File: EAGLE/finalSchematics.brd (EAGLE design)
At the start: 100 x 80 mm, 12 parts, among them IC1 STM32F103RBT, P1 DM3CS-SF, Q1 8MHz 131-220

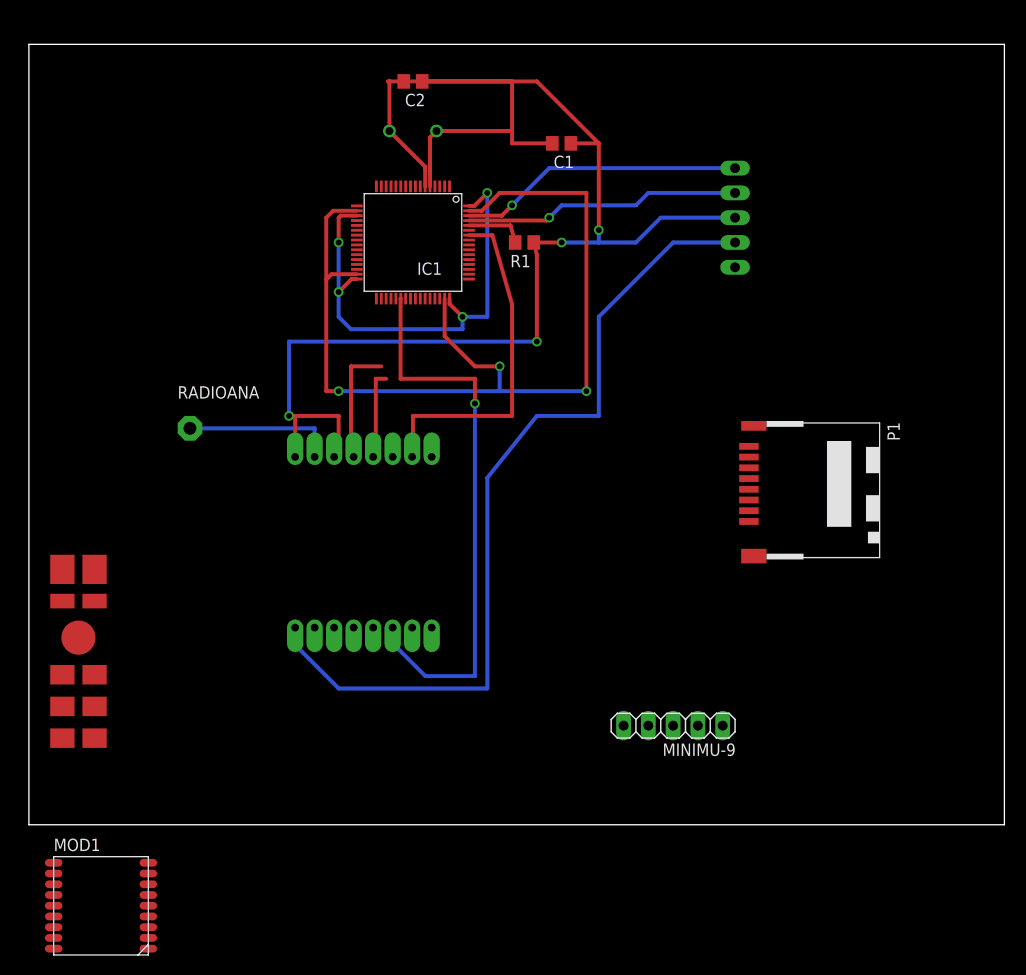
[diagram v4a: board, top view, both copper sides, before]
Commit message: Finish modules
All modules except SD card imported in the schematic. Board still to-do
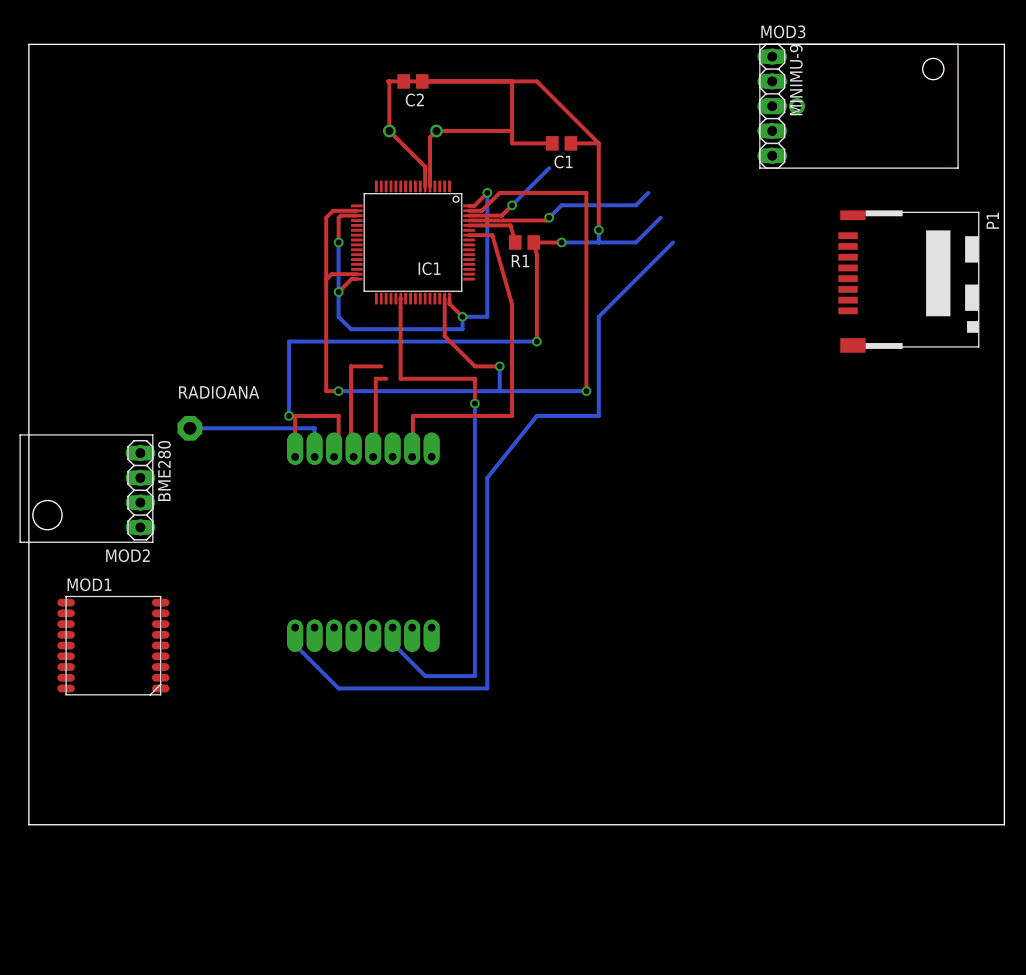
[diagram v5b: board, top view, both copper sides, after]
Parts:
- removed GPSANA: ANT-NSG4712-6, roundsolutions:ANT-NSG4712-6
- added MOD2: (no value), BME280:BME280
- added MOD3: IMU04A, IMU:IMU04A
- BME280: device pinhead:1X05/90 -> pinhead:1X04
- MOD1: value (none) -> GPS
- moved BME280 70.5 mm to (11.4, 34.3), flipped to the top, turned to 270 degrees
- moved MINIMU-9 64.3 mm to (76.2, 73.7), turned to 270 degrees
- moved MOD1 26.7 mm to (3.81, 14.0)
- moved P1 23.9 mm to (90.2, 55.9)
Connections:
- new net RX: MOD1.RXD1
- new net TX: MOD1.TXD1
- net +3V3: now also BME280.1; no longer BME280.2
- net GND: now also BME280.2; no longer BME280.3
- net SCL: now also BME280.3; no longer BME280.4
- net SDA: now also BME280.4; no longer BME280.5
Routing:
- net SDA: track 29.3 -> 10.2 mm
- net SCL: track 77.6 -> 68.7 mm
- net GND: track 113.2 -> 105.6 mm
- net +3V3: track 87.2 -> 80.8 mm
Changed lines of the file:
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@@
 <?xml version="1.0" encoding="utf-8"?>
 <!DOCTYPE eagle SYSTEM "eagle.dtd">
-<eagle version="8.0.1">
+<eagle version="8.0.0">
 <drawing>
 <settings>
@@
 <element name="R1" library="rcl" package="R0805" value="10k 901-655" x="50.8" y="59.69" rot="R180"/>
 <element name="U$1" library="RFM69mod" package="20X16BOARD" value="RFM69" x="34.29" y="29.21" rot="MR90"/>
-<element name="BME280" library="pinhead" package="1X05/90" value="" x="76.2" y="62.23" rot="MR90"/>
-<element name="GPSANA" library="roundsolutions" package="ANT-NSG4712-6" value="ANT-NSG4712-6" x="5.08" y="17.78"/>
-<element name="MINIMU-9" library="pinhead" package="1X05" value="" x="66.04" y="10.16" rot="R180"/>
-<element name="P1" library="DM3CS-SF" package="HRS_DM3CS-SF" value="DM3CS-SF" x="80.01" y="34.29" rot="R270">
-<attribute name="PRICE" value="1.04 USD" x="80.01" y="34.29" size="1.778" layer="27" rot="R270" display="off"/>
-<attribute name="DESCRIPTION" value="Conn Micro SD Card HDR 8 POS 1.1mm Solder RA SMD Embossed T/R 0.5A" x="80.01" y="34.29" size="1.778" layer="27" rot="R270" display="off"/>
-<attribute name="MP" value="DM3CS-SF" x="80.01" y="34.29" size="1.778" layer="27" rot="R270" display="off"/>
-<attribute name="AVAILABILITY" value="Good" x="80.01" y="34.29" size="1.778" layer="27" rot="R270" display="off"/>
-<attribute name="PACKAGE" value="None" x="80.01" y="34.29" size="1.778" layer="27" rot="R270" display="off"/>
-<attribute name="MF" value="Hirose" x="80.01" y="34.29" size="1.778" layer="27" rot="R270" display="off"/>
+<element name="MINIMU-9" library="pinhead" package="1X05" value="" x="76.2" y="73.66" rot="R270"/>
+<element name="P1" library="DM3CS-SF" package="HRS_DM3CS-SF" value="DM3CS-SF" x="90.17" y="55.88" rot="R270">
+<attribute name="PRICE" value="1.04 USD" x="90.17" y="55.88" size="1.778" layer="27" rot="R270" display="off"/>
+<attribute name="DESCRIPTION" value="Conn Micro SD Card HDR 8 POS 1.1mm Solder RA SMD Embossed T/R 0.5A" x="90.17" y="55.88" size="1.778" layer="27" rot="R270" display="off"/>
+<attribute name="MP" value="DM3CS-SF" x="90.17" y="55.88" size="1.778" layer="27" rot="R270" display="off"/>
+<attribute name="AVAILABILITY" value="Good" x="90.17" y="55.88" size="1.778" layer="27" rot="R270" display="off"/>
+<attribute name="PACKAGE" value="None" x="90.17" y="55.88" size="1.778" layer="27" rot="R270" display="off"/>
+<attribute name="MF" value="Hirose" x="90.17" y="55.88" size="1.778" layer="27" rot="R270" display="off"/>
 </element>
-<element name="MOD1" library="components" package="L70B-GPS" value="" x="2.54" y="-12.7"/>
+<element name="MOD1" library="components" package="L70B-GPS" value="GPS" x="3.81" y="13.97"/>
+<element name="MOD2" library="BME280" package="BME280" value="" x="12.7" y="39.37" rot="R180"/>
+<element name="BME280" library="pinhead" package="1X04" value="" x="11.43" y="34.29" rot="R270"/>
+<element name="MOD3" library="IMU" package="IMU04A" value="IMU04A" x="76.2" y="73.66"/>
 </elements>
 <signals>
@@
 <wire x1="26.67" y1="49.53" x2="26.67" y2="41.91" width="0.4064" layer="16"/>
 <via x="26.67" y="41.91" extent="1-16" drill="0.6"/>
-<contactref element="BME280" pad="3"/>
 <via x="52.07" y="49.53" extent="1-16" drill="0.6" shape="square"/>
 <wire x1="52.07" y1="58.42" x2="51.75" y2="59.69" width="0.4064" layer="1"/>
@@
 <wire x1="58.42" y1="59.69" x2="62.23" y2="59.69" width="0.4064" layer="16"/>
 <wire x1="62.23" y1="59.69" x2="64.77" y2="62.23" width="0.4064" layer="16"/>
-<wire x1="64.77" y1="62.23" x2="72.39" y2="62.23" width="0.4064" layer="16"/>
 <wire x1="58.42" y1="59.69" x2="58.42" y2="60.96" width="0.4064" layer="16"/>
 <via x="58.42" y="60.96" extent="1-16" drill="0.6" shape="square"/>
@@
 <contactref element="MINIMU-9" pad="3"/>
 <contactref element="P1" pad="6"/>
+<contactref element="BME280" pad="2"/>
+<contactref element="MOD1" pad="GND2"/>
 <contactref element="MOD1" pad="GND1"/>
-<contactref element="MOD1" pad="GND2"/>
 <contactref element="MOD1" pad="GND3"/>
-<wire x1="52.07" y1="49.53" x2="73.81" y2="36.59" width="0" layer="19" extent="1-1"/>
-<wire x1="66.04" y1="10.16" x2="73.81" y2="36.59" width="0" layer="19" extent="1-1"/>
-<wire x1="2.54" y1="-3.9" x2="27.29" y2="37.71" width="0" layer="19" extent="1-1"/>
-<wire x1="2.54" y1="-6.1" x2="2.54" y2="-3.9" width="0" layer="19" extent="1-1"/>
-<wire x1="12.24" y1="-12.7" x2="2.54" y2="-6.1" width="0" layer="19" extent="1-1"/>
+<wire x1="52.07" y1="49.53" x2="83.97" y2="58.18" width="0" layer="19" extent="1-1"/>
+<wire x1="76.2" y1="73.66" x2="83.97" y2="58.18" width="0" layer="19" extent="1-1"/>
+<wire x1="3.81" y1="22.77" x2="27.29" y2="37.71" width="0" layer="19" extent="1-1"/>
+<wire x1="3.81" y1="20.57" x2="3.81" y2="22.77" width="0" layer="19" extent="1-1"/>
+<wire x1="13.51" y1="13.97" x2="3.81" y2="20.57" width="0" layer="19" extent="1-1"/>
+<wire x1="11.43" y1="35.56" x2="13.51" y2="13.97" width="0" layer="19" extent="1-1"/>
 </signal>
 <signal name="NC">
@@
 <signal name="+3V3">
 <contactref element="U$1" pad="3.3V"/>
-<contactref element="BME280" pad="2"/>
-<wire x1="72.39" y1="59.69" x2="66.04" y2="59.69" width="0.4064" layer="16"/>
 <wire x1="66.04" y1="59.69" x2="58.42" y2="52.07" width="0.4064" layer="16"/>
 <wire x1="58.42" y1="52.07" x2="58.42" y2="41.91" width="0.4064" layer="16"/>
@@
 <contactref element="P1" pad="4"/>
 <contactref element="MINIMU-9" pad="5"/>
-<wire x1="60.96" y1="10.16" x2="73.81" y2="34.39" width="0" layer="19" extent="1-1"/>
-<wire x1="33.02" y1="13.97" x2="60.96" y2="10.16" width="0" layer="19" extent="16-16"/>
+<contactref element="BME280" pad="1"/>
+<wire x1="58.42" y1="41.91" x2="83.97" y2="55.98" width="0" layer="19" extent="1-16"/>
+<wire x1="76.2" y1="68.58" x2="46.99" y2="13.97" width="0" layer="19" extent="16-16"/>
+<wire x1="11.43" y1="38.1" x2="31.75" y2="13.97" width="0" layer="19" extent="16-16"/>
 </signal>
 <signal name="SCL">
@@
 <contactref element="MINIMU-9" pad="1"/>
 <contactref element="IC1" pad="61"/>
-<contactref element="BME280" pad="4"/>
 <wire x1="45.12" y1="61.94" x2="53.05" y2="61.94" width="0.4064" layer="1"/>
 <wire x1="53.05" y1="61.94" x2="53.34" y2="62.23" width="0.4064" layer="1"/>
@@
 <wire x1="54.61" y1="63.5" x2="62.23" y2="63.5" width="0.4064" layer="16"/>
 <wire x1="62.23" y1="63.5" x2="63.5" y2="64.77" width="0.4064" layer="16"/>
-<wire x1="63.5" y1="64.77" x2="72.39" y2="64.77" width="0.4064" layer="16"/>
+<contactref element="BME280" pad="3"/>
 <wire x1="45.12" y1="63.44" x2="45.12" y2="61.94" width="0" layer="19" extent="1-1"/>
-<wire x1="71.12" y1="10.16" x2="33.02" y2="50.8" width="0" layer="19" extent="16-16"/>
+<wire x1="76.2" y1="78.74" x2="46.99" y2="52.07" width="0" layer="19" extent="16-16"/>
+<wire x1="11.43" y1="33.02" x2="76.2" y2="78.74" width="0" layer="19" extent="1-1"/>
 </signal>
 <signal name="SDA">
 <contactref element="MINIMU-9" pad="2"/>
 <contactref element="IC1" pad="62"/>
-<contactref element="BME280" pad="5"/>
 <wire x1="45.12" y1="62.44" x2="48.47" y2="62.44" width="0.4064" layer="1"/>
 <wire x1="48.47" y1="62.44" x2="49.53" y2="63.5" width="0.4064" layer="1"/>
 <via x="49.53" y="63.5" extent="1-16" drill="0.6" shape="square"/>
 <wire x1="49.53" y1="63.5" x2="53.34" y2="67.31" width="0.4064" layer="16"/>
-<wire x1="53.34" y1="67.31" x2="72.39" y2="67.31" width="0.4064" layer="16"/>
-<wire x1="68.58" y1="10.16" x2="45.12" y2="62.44" width="0" layer="19" extent="1-1"/>
+<contactref element="BME280" pad="4"/>
+<wire x1="76.2" y1="76.2" x2="48.47" y2="62.44" width="0" layer="19" extent="1-1"/>
+<wire x1="11.43" y1="30.48" x2="76.2" y2="76.2" width="0" layer="19" extent="1-1"/>
 </signal>
 <signal name="MOSI">
 <contactref element="P1" pad="3"/>
 <contactref element="IC1" pad="36"/>
-<wire x1="73.81" y1="33.29" x2="37.12" y2="53.94" width="0" layer="19" extent="1-1"/>
+<wire x1="83.97" y1="54.88" x2="37.12" y2="53.94" width="0" layer="19" extent="1-1"/>
 </signal>
 <signal name="SCK">
 <contactref element="P1" pad="5"/>
 <contactref element="IC1" pad="34"/>
-<wire x1="73.81" y1="35.49" x2="36.12" y2="53.94" width="0" layer="19" extent="1-1"/>
+<wire x1="83.97" y1="57.08" x2="36.12" y2="53.94" width="0" layer="19" extent="1-1"/>
 </signal>
 <signal name="MISO">
 <contactref element="P1" pad="7"/>
 <contactref element="IC1" pad="35"/>
-<wire x1="73.81" y1="37.69" x2="36.62" y2="53.94" width="0" layer="19" extent="1-1"/>
+<wire x1="83.97" y1="59.28" x2="36.62" y2="53.94" width="0" layer="19" extent="1-1"/>
 </signal>
 <signal name="CS">
 <contactref element="P1" pad="2"/>
 <contactref element="IC1" pad="43"/>
-<wire x1="40.62" y1="53.94" x2="73.81" y2="32.19" width="0" layer="19" extent="1-1"/>
+<wire x1="40.62" y1="53.94" x2="83.97" y2="53.78" width="0" layer="19" extent="1-1"/>
 </signal>
 <signal name="VCC">
 <contactref element="MOD1" pad="VCC"/>
 </signal>
+<signal name="RX">
+<contactref element="MOD1" pad="RXD1"/>
+</signal>
+<signal name="TX">
+<contactref element="MOD1" pad="TXD1"/>
+</signal>
 </signals>
